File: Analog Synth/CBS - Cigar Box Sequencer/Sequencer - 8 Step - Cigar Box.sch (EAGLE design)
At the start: 204 parts, among them IC1 TL084P, IC10 79L05, IC11 MCP6002, IC12 74AC138N, IC13 74ALS04N, IC14 74AC138N, IC15 74ALS04N, IC16 74ALS04N, IC2 TL084P, IC3 TL084P, IC4 74ALS04N, IC5 4050N, IC6 78L05, IC7 40193N, IC8 78L05, IC9 74LS86N, Q1 I/O, Q14 J310, Q15 J310, Q16 J310, Q17 J310, Q18 J310, Q19 J310, Q2 I/O, Q20 J310, Q3 I/O, Q4 2N3906, Q5 2N3904, Q6 J310, X1 I/O, X2 I/O, X3 I/O

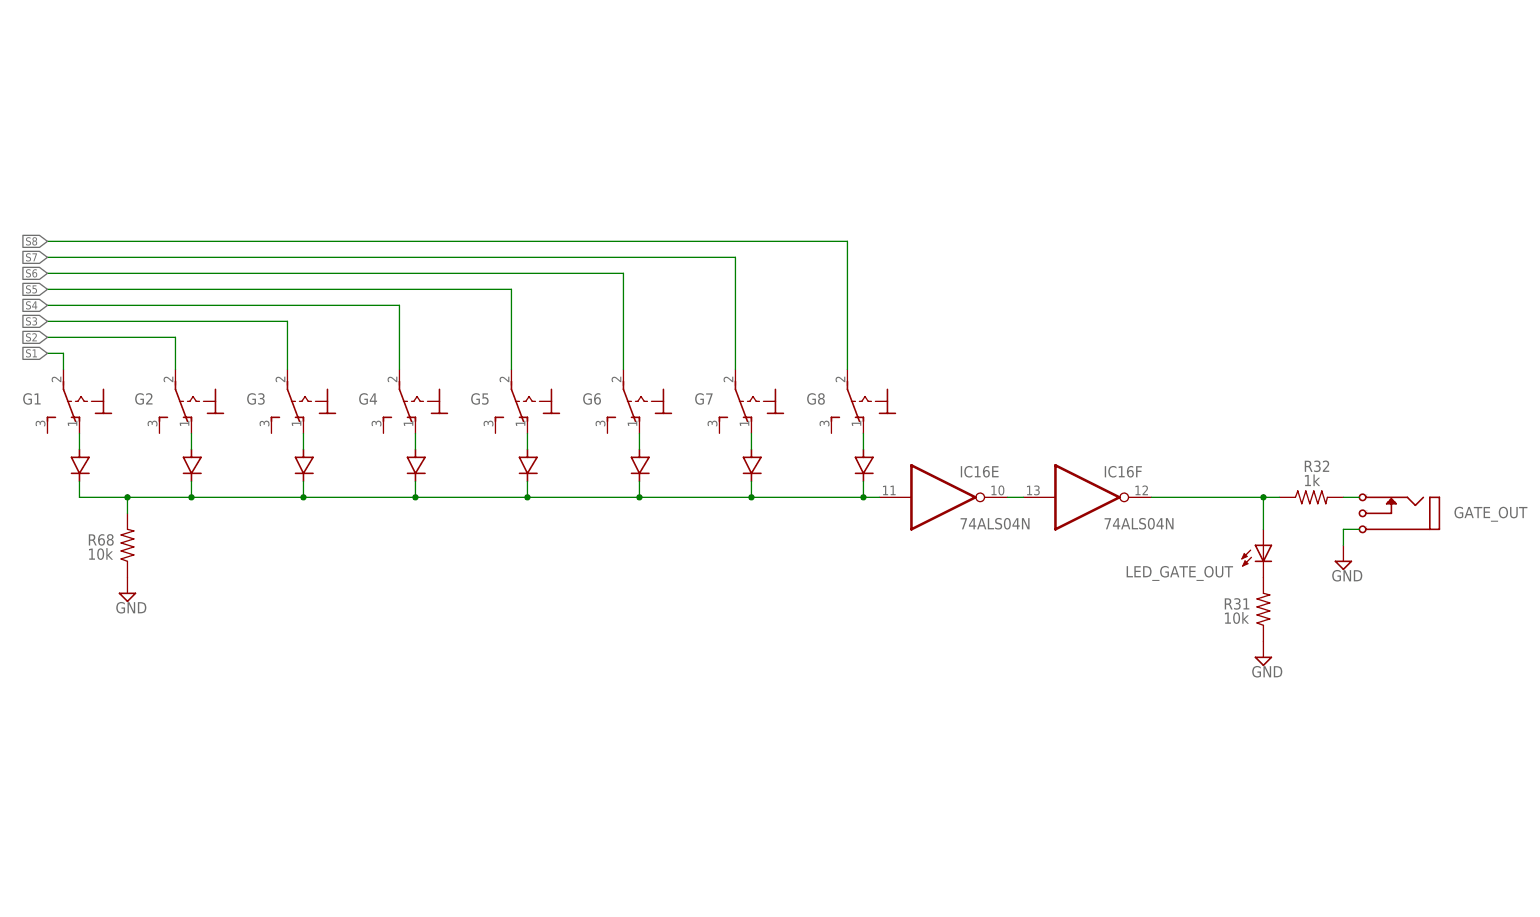
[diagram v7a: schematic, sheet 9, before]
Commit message: CBS: updating schematic to make the GATE_OUT work properly
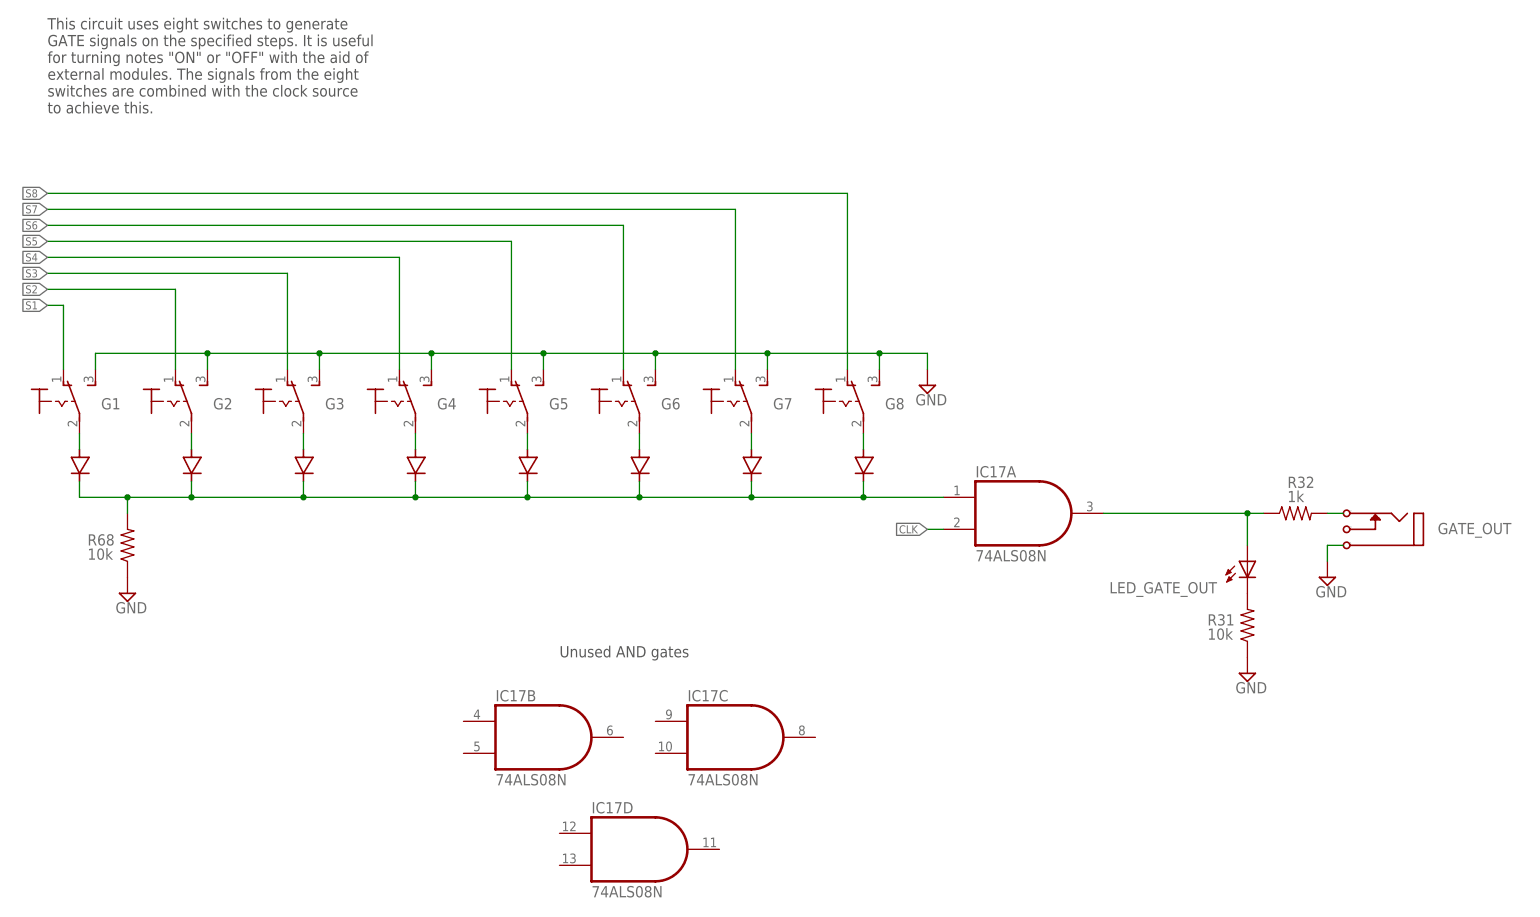
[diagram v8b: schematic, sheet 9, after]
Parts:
- added IC17: 74ALS08N, 74xx-us:74ALS08N
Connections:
- removed net N$124: IC16E.O, IC16F.I
- removed net N$134: G2.O, U$12.ANODE
- removed net N$135: G3.O, U$14.ANODE
- removed net N$136: G4.O, U$15.ANODE
- removed net N$137: G5.O, U$16.ANODE
- removed net N$138: G6.O, U$17.ANODE
- removed net N$139: G7.O, U$18.ANODE
- removed net N$140: G8.O, U$19.ANODE
- new net N$126: G8.P, U$19.ANODE
- new net N$127: G7.P, U$18.ANODE
- new net N$128: G6.P, U$17.ANODE
- new net N$129: G5.P, U$16.ANODE
- new net N$130: G4.P, U$15.ANODE
- new net N$131: G3.P, U$14.ANODE
- new net N$132: G2.P, U$12.ANODE
- net CLK: now also IC17A.I1
- net COMBINED-GATE-SIGNAL-AFAEVIRO: no longer IC16F.O
- net GND: now also G1.S, G2.S, G3.S, G4.S, G5.S, G6.S, G7.S, G8.S
- net N$133: now also G1.P; no longer G1.O
- net N$141: now also IC17A.I0; no longer IC16E.I
- net S1: now also G1.O; no longer G1.P
- net S2: now also G2.O; no longer G2.P
- net S3: now also G3.O; no longer G3.P
- net S4: now also G4.O; no longer G4.P
- net S5: now also G5.O; no longer G5.P
- net S6: now also G6.O; no longer G6.P
- net S7: now also G7.O; no longer G7.P
- net S8: now also G8.O; no longer G8.P
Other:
- note added: "2015-November"
- note added: "A 3-to-8-step sequencer built into a cigar box"
- note added: "CBS Cigar Box Sequencer"
- note added: "Eurorack Power Input"
- note added: "Number of Steps Indicator"
- note added: "Ryan Jensen"
- note added: "The Q1, Q2, and Q3 outputs allow the user to see the state of the binary counter, as well as utilize the signals it outputs."
- note added: "The X1, X2, and X3 inputs allow the user to substitude the binary counter outputs with other digital signals. This allows the user to externally specify the step the sequencer is on. With a single digital input plugged into X1, X2, or X3, the user can control the sequencer to switch between two different 4-step sequences. Additionally, with two digital signals plugged into X1, X2, or X3, the user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"
- note added: "The binary counter counts the clock signal. When the reset (clear) input goes HIGH, the binary counter resets to 0."
- note added: "The demultiplexer converts the three digital binary lines (where all each of the three lines can be either HIGH or LOW) into eight digital output lines (where only a single output is "SELECTED"). This circuit converts the binary encoding into a selection of a single step of the sequencer."
- note added: "The digital ICs and the analog circuits are powered with a seperate 5 V source"
- note added: "This circuit buffers the CV signal from the eight potentiometers. It also acts as an RC lowpass filter with a variable cutoff frequency (variable time constant)."
- note added: "This circuit is a collection of eight analog switches. They connect or disconnect the wiper of each pot to a common point called "CV_UNBUF". Only one of these switches will be activated at a time because they are controlled by the demultiplexer."
- note added: "This circuit uses eight switches to generate GATE signals on the specified steps. It is useful for turning notes "ON" or "OFF" with the aid of external modules. The signals from the eight switches are combined with the clock source to achieve this."
- note added: "This switch allows the user to manually advance through the steps of the sequencer. The circuitry around the switch debounces the signal to prevent the rapid addition of counts that occurs when a noisy switch is fed into a digital logic device."
- note added: "This switch selects between three clock sources: - Internal VCO - Internal VCO XOR'd with the External Clock - External Clock input"
- note added: "This switch selects the number of steps in the sequence and displays it on the seven- segment LED display"
- note added: "Unused AND gates"
- note added: "Unused inverters"
- note added: "Unused op amp"
- note added: "Unused op amps"
- moved on the sheet: G1, G2, G3, G4, G5, G6, G7, G8, GATE_OUT, IC11B, IC12P, IC13P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
